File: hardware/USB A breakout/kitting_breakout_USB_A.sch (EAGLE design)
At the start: 5 parts, among them J3 USB_A

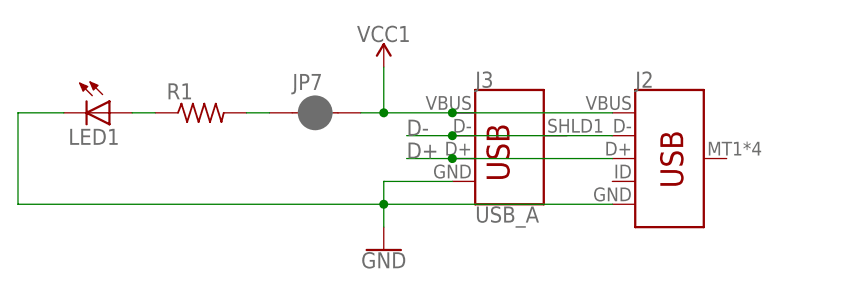
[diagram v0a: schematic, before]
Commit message: Added mounting hole on USB A breakout
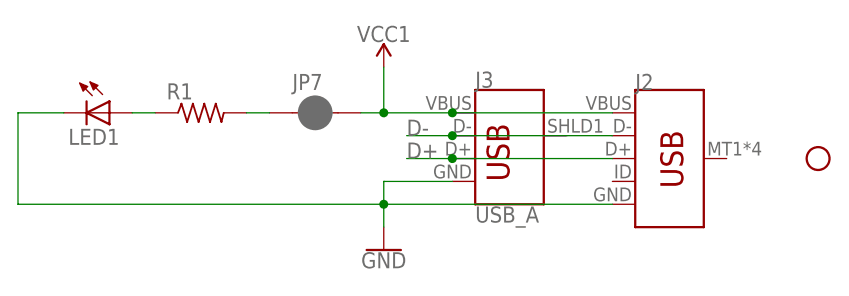
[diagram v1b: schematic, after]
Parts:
- added H1: STAND-OFF, SparkFun-Hardware:STAND-OFF
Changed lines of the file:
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@@
 <part name="J2" library="SparkFun-Connectors" deviceset="USB_MICRO-B" device="_SMT"/>
 <part name="J3" library="USB_A_female_VRT" deviceset="USB_A" device=""/>
+<part name="H1" library="SparkFun-Hardware" deviceset="STAND-OFF" device=""/>
 </parts>
 <sheets>
@@
 <instance part="J2" gate="G$1" x="15.24" y="45.72"/>
 <instance part="J3" gate="G$1" x="0" y="45.72"/>
+<instance part="H1" gate="G$1" x="33.02" y="45.72"/>
 </instances>
 <busses>
